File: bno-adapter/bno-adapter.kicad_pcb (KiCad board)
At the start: 2 copper layers, 38.7 x 31.2 mm, 15 parts, among them P1 CONN_02X05, P2 CONN_01X04, P3 CONN_01X06, P4 CONN_01X01, P5 CONN_01X01, P6 CONN_01X01, P7 CONN_01X01

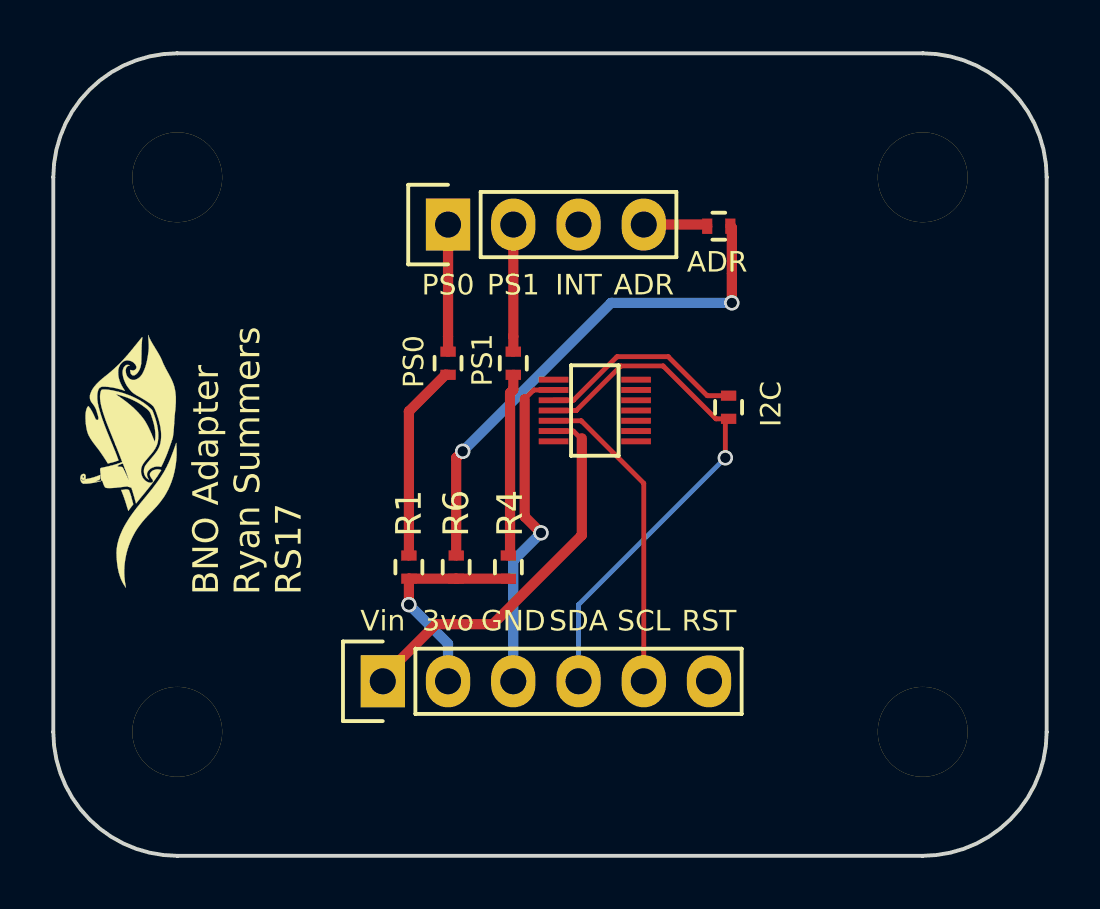
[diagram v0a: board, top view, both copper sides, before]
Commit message: Correction of BNO to new mezzanine
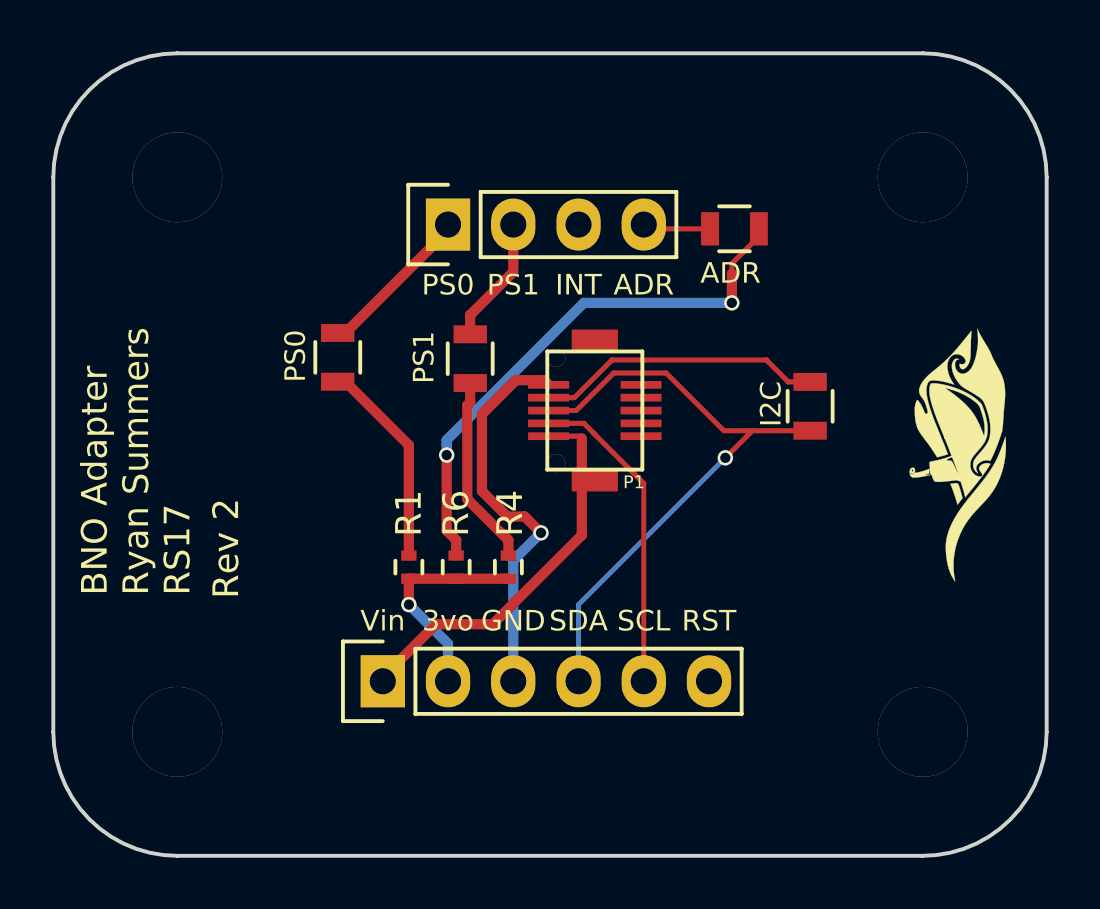
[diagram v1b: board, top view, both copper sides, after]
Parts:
- P1: value CONN_02X05 -> Mezzanine-Header; footprint robosub_footprints:DF40C-10DP-Header -> robosub_footprints:3mm-10pos-receptacle
- P4, P5, P6, P7: value CONN_01X01 -> Spacer; footprint robosub_footprints:1.5mm-spacer -> robosub_footprints:3mm-spacer
- R2, R3, R5, R7: footprint Resistors_SMD:R_0402 -> Resistors_SMD:R_0805
- moved G*** 32.3 mm to (162.3, 142.6)
- moved R3 10.2 mm to (143.2, 138.9), turned to 90 degrees
- moved R5 10.1 mm to (153.5, 133.8), turned to 180 degrees
- moved R7 7.86 mm to (156.5, 140.7), turned to 270 degrees
- moved R2 4.30 mm to (138.1, 138.8)
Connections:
- R3 pad 1: /SDA_1 -> Net-(R3-Pad1)
- R3 pad 2: /RX/SDA_0 -> /PS1
- R4 pad 2: Net-(R4-Pad2) -> Net-(R3-Pad1)
- R5 pad 1: Net-(R4-Pad2) -> Net-(R5-Pad1)
- R5 pad 2: /PS1 -> /ADR
- R6 pad 2: Net-(R6-Pad2) -> Net-(R5-Pad1)
- R7 pad 1: Net-(R6-Pad2) -> /SDA_1
- R7 pad 2: /ADR -> /RX/SDA_0
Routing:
- net Net-(R5-Pad1): track 0.00 -> 21.3 mm, vias 0 -> 2
- net Net-(R6-Pad2): track 20.0 -> 0.00 mm, vias 2 -> 0
- net Net-(R3-Pad1): track 0.00 -> 7.52 mm
- net Net-(R4-Pad2): track 7.12 -> 0.00 mm
- net /RX/SDA_0: track 21.0 -> 24.1 mm
- net /SDA_1: track 8.14 -> 11.1 mm
- net GND: track 13.0 -> 15.4 mm
- net /PS0: track 4.95 -> 6.17 mm
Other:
- net class Default: trace_width 0.4 -> 0.2
- board text added: "Rev 2"
